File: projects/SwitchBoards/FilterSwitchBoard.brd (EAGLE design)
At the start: 18.7 x 14.6 mm, 9 parts

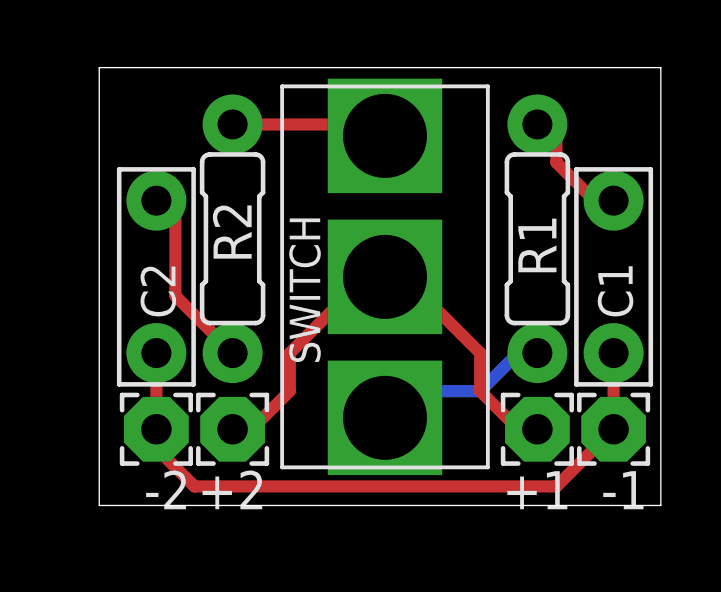
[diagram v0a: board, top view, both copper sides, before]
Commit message: Pass OSHPark DRC.
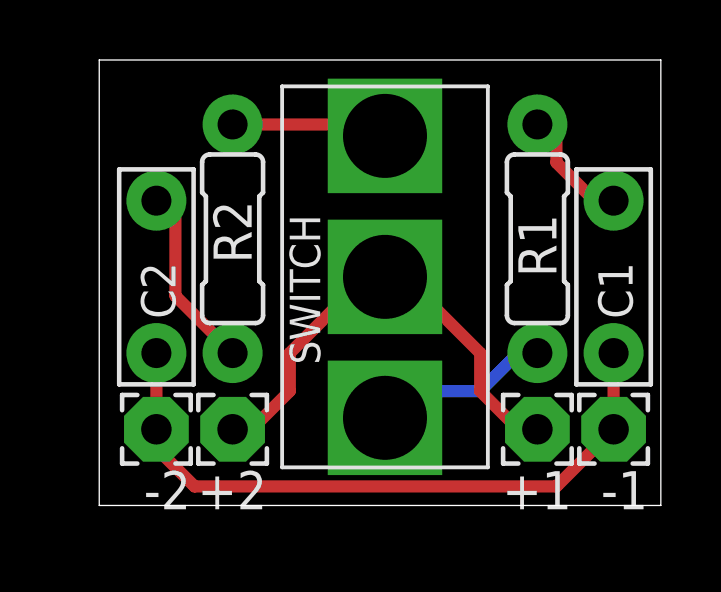
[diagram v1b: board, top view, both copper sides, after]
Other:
- board size 18.7 x 14.6 mm -> 18.7 x 14.8 mm
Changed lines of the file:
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@@
 <setting verticaltext="up"/>
 </settings>
-<grid distance="0.1" unitdist="inch" unit="inch" style="lines" multiple="1" display="yes" altdistance="0.025" altunitdist="inch" altunit="inch"/>
+<grid distance="0.1" unitdist="inch" unit="inch" style="lines" multiple="1" display="yes" altdistance="0.005" altunitdist="inch" altunit="inch"/>
 <layers>
 <layer number="1" name="Top" color="4" fill="1" visible="yes" active="yes"/>
@@
 <plain>
 <wire x1="0" y1="64.77" x2="18.72" y2="64.77" width="0" layer="20"/>
-<wire x1="18.72" y1="64.77" x2="18.72" y2="79.365" width="0" layer="20"/>
-<wire x1="18.72" y1="79.365" x2="0" y2="79.365" width="0" layer="20"/>
-<wire x1="0" y1="79.365" x2="0" y2="64.77" width="0" layer="20"/>
+<wire x1="18.72" y1="64.77" x2="18.72" y2="79.619" width="0" layer="20"/>
+<wire x1="18.72" y1="79.619" x2="0" y2="79.619" width="0" layer="20"/>
+<wire x1="0" y1="79.619" x2="0" y2="64.77" width="0" layer="20"/>
 <text x="7.62" y="78.105" size="1.016" layer="22" rot="MR270">FilterSwitchBoard</text>
 <text x="11.43" y="66.04" size="1.016" layer="22" rot="MR90">GJCAMANN2014</text>
@@
 </class>
 </classes>
-<designrules name="SparkFun">
-<description language="en">&lt;b&gt;EAGLE Design Rules&lt;/b&gt;
+<designrules name="OSHParkLaenPCBOrder">
+<description language="de">&lt;b&gt;EAGLE Design Rules&lt;/b&gt;
 &lt;p&gt;
-The default Design Rules have been set to cover
-a wide range of applications. Your particular design
-may have different requirements, so please make the
-necessary adjustments and save your customized
-design rules under a new name.</description>
+Die Standard-Design-Rules sind so gewählt, dass sie für
+die meisten Anwendungen passen. Sollte ihre Platine
+besondere Anforderungen haben, treffen Sie die erforderlichen
+Einstellungen hier und speichern die Design Rules unter
+einem neuen Namen ab.</description>
+<description language="en">&lt;b&gt;Laen's PCB Order Design Rules&lt;/b&gt;
+&lt;p&gt;
+Please make sure your boards conform to these design rules.</description>
 <param name="layerSetup" value="(1*16)"/>
-<param name="mtCopper" value="0.035mm 0.035mm 0.035mm 0.035mm 0.035mm 0.035mm 0.035mm 0.035mm 0.035mm 0.035mm 0.035mm 0.035mm 0.035mm 0.035mm 0.035mm 0.035mm"/>
-<param name="mtIsolate" value="1.5mm 0.15mm 0.2mm 0.15mm 0.2mm 0.15mm 0.2mm 0.15mm 0.2mm 0.15mm 0.2mm 0.15mm 0.2mm 0.15mm 0.2mm"/>
-<param name="mdWireWire" value="8mil"/>
-<param name="mdWirePad" value="8mil"/>
-<param name="mdWireVia" value="8mil"/>
-<param name="mdPadPad" value="8mil"/>
-<param name="mdPadVia" value="8mil"/>
-<param name="mdViaVia" value="8mil"/>
-<param name="mdSmdPad" value="8mil"/>
-<param name="mdSmdVia" value="8mil"/>
-<param name="mdSmdSmd" value="8mil"/>
+<param name="mtCopper" value="0.0356mm 0.0356mm 0.0356mm 0.0356mm 0.0356mm 0.0356mm 0.0356mm 0.0356mm 0.0356mm 0.0356mm 0.0356mm 0.0356mm 0.0356mm 0.0356mm 0.0356mm 0.0356mm"/>
+<param name="mtIsolate" value="1.5011mm 0.1499mm 0.2007mm 0.1499mm 0.2007mm 0.1499mm 0.2007mm 0.1499mm 0.2007mm 0.1499mm 0.2007mm 0.1499mm 0.2007mm 0.1499mm 0.2007mm"/>
+<param name="mdWireWire" value="6mil"/>
+<param name="mdWirePad" value="6mil"/>
+<param name="mdWireVia" value="6mil"/>
+<param name="mdPadPad" value="6mil"/>
+<param name="mdPadVia" value="6mil"/>
+<param name="mdViaVia" value="6mil"/>
+<param name="mdSmdPad" value="6mil"/>
+<param name="mdSmdVia" value="6mil"/>
+<param name="mdSmdSmd" value="6mil"/>
 <param name="mdViaViaSameLayer" value="8mil"/>
 <param name="mnLayersViaInSmd" value="2"/>
-<param name="mdCopperDimension" value="10mil"/>
-<param name="mdDrill" value="8mil"/>
+<param name="mdCopperDimension" value="15mil"/>
+<param name="mdDrill" value="6mil"/>
 <param name="mdSmdStop" value="0mil"/>
-<param name="msWidth" value="8mil"/>
-<param name="msDrill" value="20mil"/>
-<param name="msMicroVia" value="9.99mm"/>
+<param name="msWidth" value="6mil"/>
+<param name="msDrill" value="13mil"/>
+<param name="msMicroVia" value="13mil"/>
 <param name="msBlindViaRatio" value="0.5"/>
 <param name="rvPadTop" value="0.25"/>
@@
 <param name="rvMicroViaOuter" value="0.25"/>
 <param name="rvMicroViaInner" value="0.25"/>
-<param name="rlMinPadTop" value="12mil"/>
+<param name="rlMinPadTop" value="7mil"/>
 <param name="rlMaxPadTop" value="20mil"/>
-<param name="rlMinPadInner" value="10mil"/>
+<param name="rlMinPadInner" value="7mil"/>
 <param name="rlMaxPadInner" value="20mil"/>
-<param name="rlMinPadBottom" value="12mil"/>
+<param name="rlMinPadBottom" value="7mil"/>
 <param name="rlMaxPadBottom" value="20mil"/>
-<param name="rlMinViaOuter" value="10mil"/>
+<param name="rlMinViaOuter" value="7mil"/>
 <param name="rlMaxViaOuter" value="20mil"/>
-<param name="rlMinViaInner" value="10mil"/>
+<param name="rlMinViaInner" value="7mil"/>
 <param name="rlMaxViaInner" value="20mil"/>
 <param name="rlMinMicroViaOuter" value="4mil"/>
@@
 <param name="mvStopFrame" value="1"/>
 <param name="mvCreamFrame" value="0"/>
-<param name="mlMinStopFrame" value="4mil"/>
-<param name="mlMaxStopFrame" value="4mil"/>
+<param name="mlMinStopFrame" value="3mil"/>
+<param name="mlMaxStopFrame" value="3mil"/>
 <param name="mlMinCreamFrame" value="0mil"/>
 <param name="mlMaxCreamFrame" value="0mil"/>
-<param name="mlViaStopLimit" value="25mil"/>
+<param name="mlViaStopLimit" value="0mil"/>
 <param name="srRoundness" value="0"/>
 <param name="srMinRoundness" value="0mil"/>

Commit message: Final project updates. Ready to send to oshpark.
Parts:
- moved C1 3.05 mm to (17.1, 75.4)
- moved C2 3.05 mm to (1.91, 75.4)
- moved R1 0.51 mm to (14.6, 74.2)
- moved R2 0.51 mm to (4.45, 74.2)
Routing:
- net N$5: track 22.3 -> 27.9 mm
- net N$3: track 6.50 -> 8.67 mm
- net N$2: track 4.34 -> 2.54 mm
- net N$7: track 15.9 -> 14.4 mm
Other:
- board size 18.7 x 14.8 mm -> 18.5 x 14.3 mm
- board text added: "GJCAMANN(C)2014"
- board text added: "V1.0"
- board text removed: "GJCAMANN2014"
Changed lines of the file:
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@@
 <setting verticaltext="up"/>
 </settings>
-<grid distance="0.1" unitdist="inch" unit="inch" style="lines" multiple="1" display="yes" altdistance="0.005" altunitdist="inch" altunit="inch"/>
+<grid distance="0.1" unitdist="inch" unit="inch" style="lines" multiple="1" display="yes" altdistance="0.01" altunitdist="inch" altunit="inch"/>
 <layers>
 <layer number="1" name="Top" color="4" fill="1" visible="yes" active="yes"/>
@@
 <layer number="20" name="Dimension" color="15" fill="1" visible="yes" active="yes"/>
 <layer number="21" name="tPlace" color="7" fill="1" visible="yes" active="yes"/>
-<layer number="22" name="bPlace" color="7" fill="1" visible="yes" active="yes"/>
+<layer number="22" name="bPlace" color="7" fill="1" visible="no" active="yes"/>
 <layer number="23" name="tOrigins" color="15" fill="1" visible="yes" active="yes"/>
 <layer number="24" name="bOrigins" color="15" fill="1" visible="yes" active="yes"/>
@@
 <board>
 <plain>
-<wire x1="0" y1="64.77" x2="18.72" y2="64.77" width="0" layer="20"/>
-<wire x1="18.72" y1="64.77" x2="18.72" y2="79.619" width="0" layer="20"/>
-<wire x1="18.72" y1="79.619" x2="0" y2="79.619" width="0" layer="20"/>
-<wire x1="0" y1="79.619" x2="0" y2="64.77" width="0" layer="20"/>
+<wire x1="0.254" y1="65.278" x2="18.72" y2="65.278" width="0" layer="20"/>
+<wire x1="18.72" y1="65.278" x2="18.72" y2="79.619" width="0" layer="20"/>
+<wire x1="18.72" y1="79.619" x2="0.254" y2="79.619" width="0" layer="20"/>
+<wire x1="0.254" y1="79.619" x2="0.254" y2="65.278" width="0" layer="20"/>
 <text x="7.62" y="78.105" size="1.016" layer="22" rot="MR270">FilterSwitchBoard</text>
-<text x="11.43" y="66.04" size="1.016" layer="22" rot="MR90">GJCAMANN2014</text>
+<text x="11.43" y="66.04" size="1.016" layer="22" rot="MR90">GJCAMANN(C)2014</text>
+<text x="18.669" y="70.104" size="1.016" layer="22" rot="MR0">V1.0</text>
+<wire x1="5.588" y1="76.962" x2="7.112" y2="76.962" width="0.4064" layer="21"/>
+<wire x1="6.604" y1="77.47" x2="7.112" y2="76.962" width="0.4064" layer="21"/>
+<wire x1="7.112" y1="76.962" x2="6.604" y2="76.454" width="0.4064" layer="21"/>
+<wire x1="13.208" y1="67.818" x2="11.684" y2="67.818" width="0.4064" layer="21"/>
+<wire x1="12.192" y1="68.326" x2="11.684" y2="67.818" width="0.4064" layer="21"/>
+<wire x1="11.684" y1="67.818" x2="12.192" y2="67.31" width="0.4064" layer="21"/>
 </plain>
 <attributes>
@@
 <elements>
 <element name="U$1" library="gc_pedal_parts" package="SPDT_SOLDER" value="SPDT_SOLDER" x="9.525" y="72.39"/>
-<element name="R1" library="resistors" package="R0207/3" value="" x="14.605" y="73.66" rot="R90"/>
-<element name="R2" library="resistors" package="R0207/3" value="" x="4.445" y="73.66" rot="R270"/>
-<element name="C1" library="capacitors-film" package="BOX_SMALL" value="" x="17.145" y="72.39" rot="R90"/>
-<element name="C2" library="capacitors-film" package="BOX_SMALL" value="" x="1.905" y="72.39" rot="R90"/>
-<element name="+2" library="wirepad" package="2,15/1,0" value="" x="4.445" y="67.31" rot="R180"/>
-<element name="-1" library="wirepad" package="2,15/1,0" value="" x="17.145" y="67.31" rot="R180"/>
-<element name="-2" library="wirepad" package="2,15/1,0" value="" x="1.905" y="67.31" rot="R180"/>
-<element name="+1" library="wirepad" package="2,15/1,0" value="" x="14.605" y="67.31" rot="R180"/>
+<element name="R1" library="resistors" package="R0207/3" value="" x="14.605" y="74.168" rot="R90"/>
+<element name="R2" library="resistors" package="R0207/3" value="" x="4.445" y="74.168" rot="R270"/>
+<element name="C1" library="capacitors-film" package="BOX_SMALL" value="" x="17.145" y="75.438" rot="R90"/>
+<element name="C2" library="capacitors-film" package="BOX_SMALL" value="" x="1.905" y="75.438" rot="R90"/>
+<element name="+2" library="wirepad" package="2,15/1,0" value="" x="4.445" y="67.31" smashed="yes" rot="R180">
+<attribute name="NAME" x="3.81" y="69.977" size="1.27" layer="25" ratio="10" rot="R180"/>
+<attribute name="VALUE" x="4.445" y="66.31" size="0.0254" layer="27" rot="R180"/>
+</element>
+<element name="-1" library="wirepad" package="2,15/1,0" value="" x="17.145" y="67.31" smashed="yes" rot="R180">
+<attribute name="NAME" x="18.288" y="69.723" size="1.27" layer="25" ratio="10" rot="R180"/>
+<attribute name="VALUE" x="17.145" y="66.31" size="0.0254" layer="27" rot="R180"/>
+</element>
+<element name="-2" library="wirepad" package="2,15/1,0" value="" x="1.905" y="67.31" smashed="yes" rot="R180">
+<attribute name="NAME" x="1.778" y="69.977" size="1.27" layer="25" ratio="10" rot="R180"/>
+<attribute name="VALUE" x="1.905" y="66.31" size="0.0254" layer="27" rot="R180"/>
+</element>
+<element name="+1" library="wirepad" package="2,15/1,0" value="" x="14.605" y="67.31" smashed="yes" rot="R180">
+<attribute name="NAME" x="16.51" y="69.723" size="1.27" layer="25" ratio="10" rot="R180"/>
+<attribute name="VALUE" x="14.605" y="66.31" size="0.0254" layer="27" rot="R180"/>
+</element>
 </elements>
 <signals>
@@
 <contactref element="U$1" pad="P$1"/>
 <contactref element="R1" pad="1"/>
-<wire x1="12.7" y1="68.58" x2="13.97" y2="69.85" width="0.4064" layer="16"/>
-<wire x1="10.16" y1="68.58" x2="12.7" y2="68.58" width="0.4064" layer="16"/>
-<wire x1="13.97" y1="69.85" x2="14.605" y2="69.85" width="0.1524" layer="16"/>
-<wire x1="10.16" y1="68.58" x2="9.525" y2="67.691" width="0.1524" layer="16"/>
+<wire x1="9.525" y1="67.691" x2="12.446" y2="67.691" width="0.4064" layer="16"/>
+<wire x1="12.446" y1="67.691" x2="14.605" y2="70.358" width="0.4064" layer="16"/>
 </signal>
 <signal name="N$2">
 <contactref element="R1" pad="2"/>
 <contactref element="C1" pad="2"/>
-<wire x1="15.24" y1="76.2" x2="16.51" y2="74.93" width="0.4064" layer="1"/>
-<wire x1="15.24" y1="77.47" x2="15.24" y2="76.2" width="0.4064" layer="1"/>
-<wire x1="16.51" y1="74.93" x2="17.145" y2="74.93" width="0.4064" layer="1"/>
-<wire x1="15.24" y1="77.47" x2="14.605" y2="77.47" width="0.1524" layer="1"/>
+<wire x1="14.605" y1="77.978" x2="17.145" y2="77.978" width="0.4064" layer="1"/>
 </signal>
 <signal name="N$3">
 <contactref element="R2" pad="2"/>
 <contactref element="C2" pad="2"/>
-<wire x1="2.54" y1="71.755" x2="3.81" y2="70.485" width="0.4064" layer="1"/>
-<wire x1="2.54" y1="74.93" x2="2.54" y2="71.755" width="0.4064" layer="1"/>
-<wire x1="3.81" y1="70.485" x2="4.445" y2="69.85" width="0.1524" layer="1"/>
-<wire x1="2.54" y1="74.93" x2="1.905" y2="74.93" width="0.1524" layer="1"/>
+<wire x1="1.905" y1="77.978" x2="4.445" y2="75.438" width="0.4064" layer="1"/>
+<wire x1="4.445" y1="75.438" x2="4.445" y2="70.358" width="0.4064" layer="1"/>
 </signal>
 <signal name="N$4">
 <contactref element="U$1" pad="P$2"/>
 <contactref element="R2" pad="1"/>
-<wire x1="8.89" y1="77.47" x2="4.445" y2="77.47" width="0.4064" layer="1"/>
-<wire x1="8.89" y1="77.47" x2="9.525" y2="77.089" width="0.4064" layer="1"/>
+<wire x1="4.445" y1="77.978" x2="8.636" y2="77.978" width="0.4064" layer="1"/>
+<wire x1="8.636" y1="77.978" x2="9.525" y2="77.089" width="0.4064" layer="1"/>
 </signal>
 <signal name="N$5">
@@
 <contactref element="-1" pad="1"/>
 <contactref element="-2" pad="1"/>
-<wire x1="1.905" y1="67.31" x2="1.905" y2="66.675" width="0.4064" layer="1"/>
-<wire x1="1.905" y1="66.675" x2="3.175" y2="65.405" width="0.4064" layer="1"/>
-<wire x1="3.175" y1="65.405" x2="15.24" y2="65.405" width="0.4064" layer="1"/>
-<wire x1="15.24" y1="65.405" x2="17.145" y2="67.31" width="0.4064" layer="1"/>
-<wire x1="1.905" y1="69.85" x2="1.905" y2="67.31" width="0.4064" layer="1"/>
-<wire x1="17.145" y1="69.85" x2="17.145" y2="67.31" width="0.4064" layer="1"/>
+<wire x1="1.905" y1="67.31" x2="1.905" y2="72.898" width="0.4064" layer="16"/>
+<wire x1="17.145" y1="72.898" x2="17.145" y2="67.31" width="0.4064" layer="16"/>
+<wire x1="1.905" y1="72.898" x2="3.683" y2="74.676" width="0.4064" layer="16"/>
+<wire x1="3.683" y1="74.676" x2="15.367" y2="74.676" width="0.4064" layer="16"/>
+<wire x1="15.367" y1="74.676" x2="17.145" y2="72.898" width="0.4064" layer="16"/>
 </signal>
 <signal name="N$7">
@@
 <contactref element="+2" pad="1"/>
 <contactref element="+1" pad="1"/>
-<wire x1="6.35" y1="68.58" x2="5.08" y2="67.31" width="0.4064" layer="1"/>
-<wire x1="6.35" y1="69.85" x2="6.35" y2="68.58" width="0.4064" layer="1"/>
-<wire x1="8.89" y1="72.39" x2="6.35" y2="69.85" width="0.4064" layer="1"/>
-<wire x1="5.08" y1="67.31" x2="4.445" y2="67.31" width="0.1524" layer="1"/>
-<wire x1="8.89" y1="72.39" x2="9.525" y2="72.39" width="0.4064" layer="1"/>
-<wire x1="12.7" y1="68.58" x2="13.97" y2="67.31" width="0.4064" layer="1"/>
-<wire x1="12.7" y1="69.85" x2="12.7" y2="68.58" width="0.4064" layer="1"/>
-<wire x1="10.16" y1="72.39" x2="12.7" y2="69.85" width="0.4064" layer="1"/>
-<wire x1="13.97" y1="67.31" x2="14.605" y2="67.31" width="0.4064" layer="1"/>
-<wire x1="10.16" y1="72.39" x2="9.525" y2="72.39" width="0.1524" layer="1"/>
+<wire x1="4.445" y1="67.31" x2="9.525" y2="72.39" width="0.4064" layer="1"/>
+<wire x1="9.525" y1="72.39" x2="14.605" y2="67.31" width="0.4064" layer="1"/>
 </signal>
 </signals>
